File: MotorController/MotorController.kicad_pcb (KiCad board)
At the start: 2 copper layers, 55 x 45 mm, 35 parts, among them J1 4P4C, J2 AVR-ISP-10, J3 8P8C, J4 Screw_Terminal_01x02, Q1 Q_NMOS_GSD, SW1 SW_SPDT, SW2 SW_Push, U1 LD1117S50TR_SOT223, U2 MAX485E, U3 ATmega8A-AU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

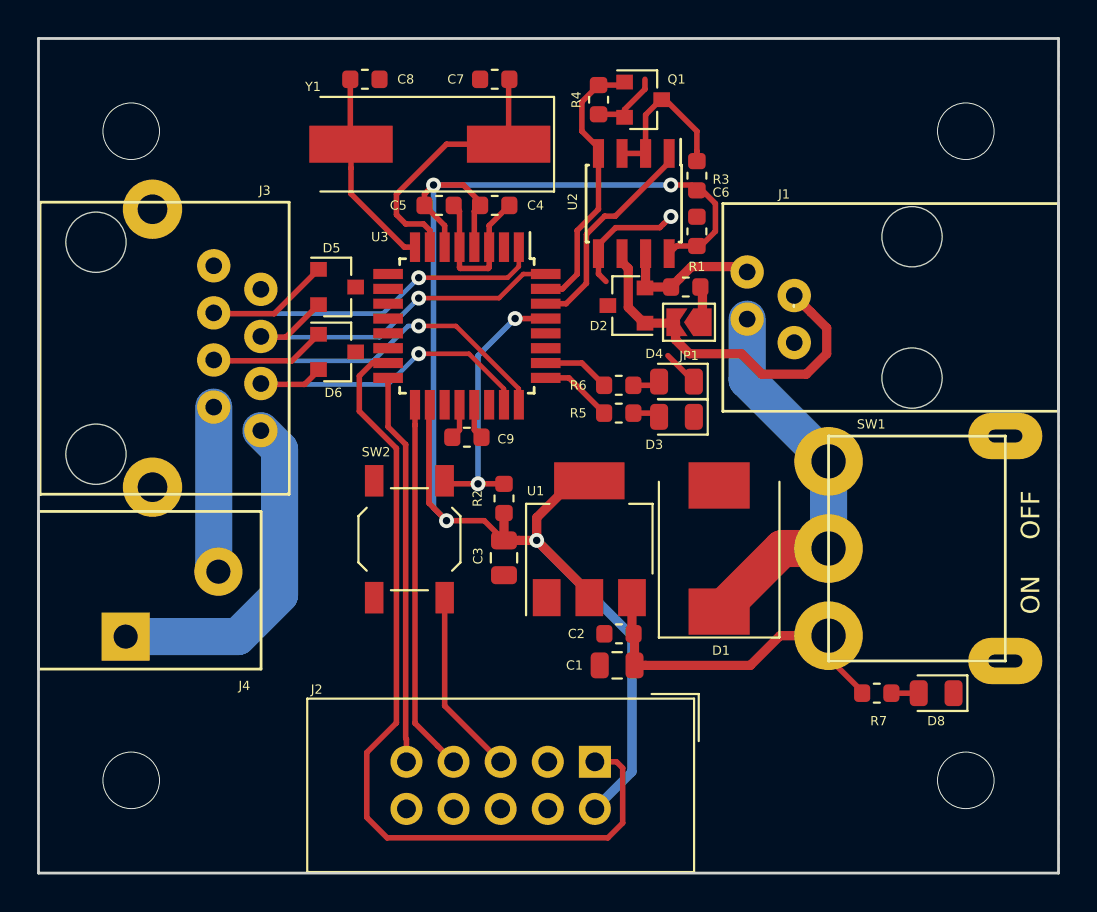
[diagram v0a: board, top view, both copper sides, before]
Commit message: First review. Fixed polygon pours, silkscreen and soldermask.
Squashed commit of the following:

commit 42a4a5d146683d2b2a8899b51cbc9eaef6797660
Author: Paweł <mackipawel@gmail.com>
Date:   Tue Apr 16 00:20:58 2019 +0200

    Changed solder mask design rules. Changed polygon pours clearence.

commit a27d25858da40b0edc55a62741cad58f571e73a1
Author: Paweł <mackipawel@gmail.com>
Date:   Sun Apr 14 15:00:25 2019 +0200

    Set via size to 0.3/0.6. Added silk screen descriptions in MotorDriver.

commit d55559f2128c74f860d75a89ad8b68139a6ba707
Author: Paweł <mackipawel@gmail.com>
Date:   Sun Apr 14 13:56:25 2019 +0200

    Added EcoTech logo in MotorController.
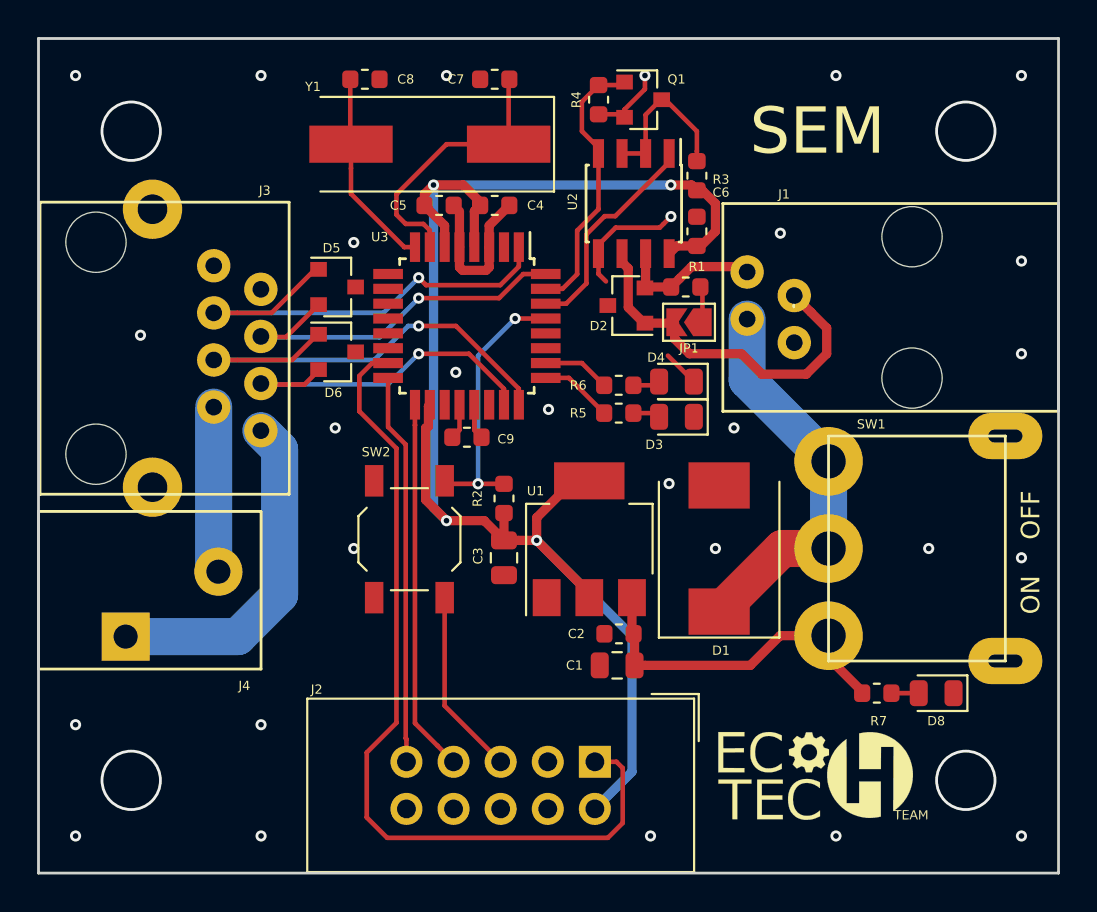
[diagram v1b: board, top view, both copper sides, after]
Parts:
- added G***: LOGO, Footprints:EcoTech, F.Cu at (117.0, 100.0)
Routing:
- net /A: track 20.1 -> 19.5 mm
- net GND: track 24.0 -> 24.1 mm, vias 1 -> 28
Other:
- net class Default: via_dia 0.8 -> 0.6; via_drill 0.4 -> 0.3
- net class Power added: clearance 0.2, trace_width 2, via_dia 0.6, via_drill 0.3
- net class Wide added: clearance 0.2, trace_width 0.5, via_dia 0.6, via_drill 0.3
- rule pad_to_mask_clearance: 0.051 -> 0.1
- rule solder_mask_min_width: 0.25 -> 0.2
- board text added: "SEM"

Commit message: Small changes in copper pours.
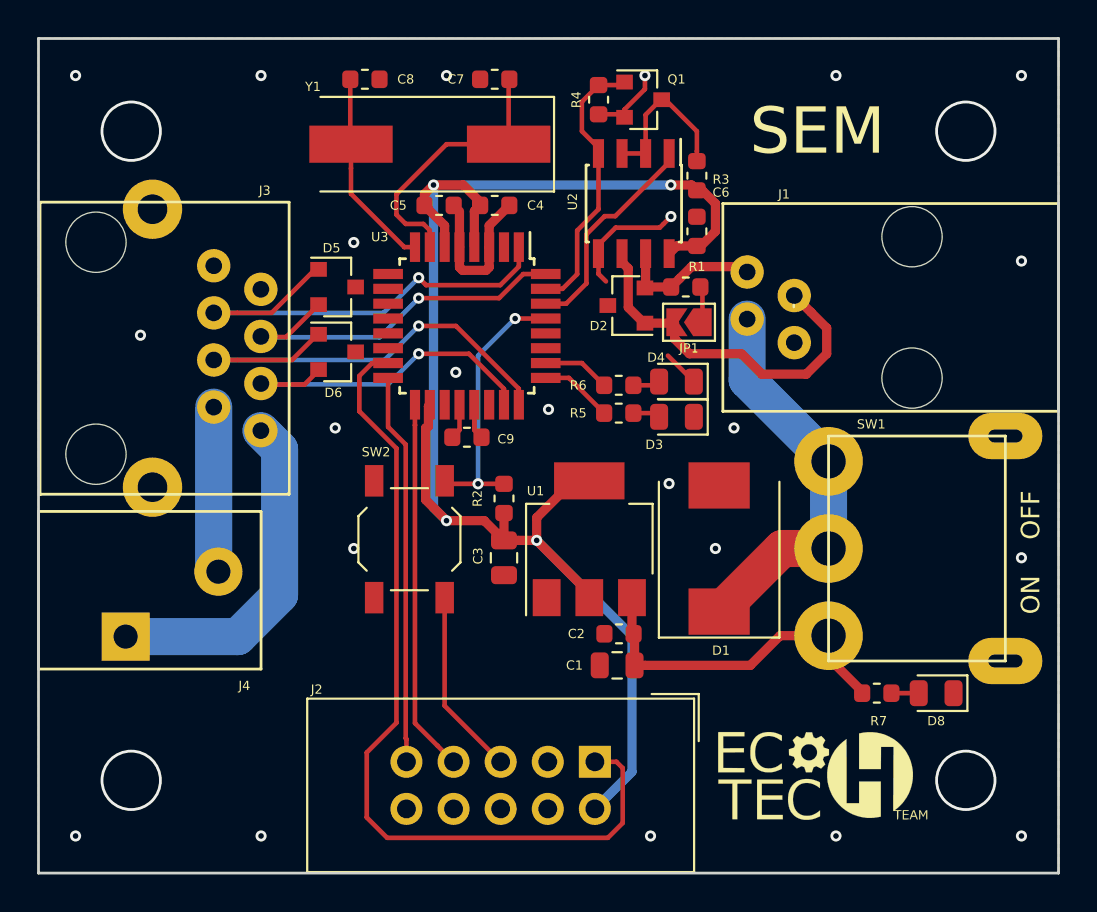
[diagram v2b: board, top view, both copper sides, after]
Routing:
- net GND: vias 28 -> 23
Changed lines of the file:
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@@
     (thickness 1.6)
     (drawings 7)
-    (tracks 284)
+    (tracks 278)
     (zones 0)
     (modules 36)
@@
   (via (at 128 88) (size 0.6) (drill 0.3) (layers F.Cu B.Cu) (net 10))
   (via (at 128 72) (size 0.6) (drill 0.3) (layers F.Cu B.Cu) (net 10))
-  (via (at 128 77) (size 0.6) (drill 0.3) (layers F.Cu B.Cu) (net 10))
   (via (at 109 84) (size 0.6) (drill 0.3) (layers F.Cu B.Cu) (net 10))
   (via (at 112.5 81) (size 0.6) (drill 0.3) (layers F.Cu B.Cu) (net 10))
   (via (at 111.5 87.5) (size 0.6) (drill 0.3) (layers F.Cu B.Cu) (net 10))
-  (via (at 123 87.5) (size 0.6) (drill 0.3) (layers F.Cu B.Cu) (net 10))
-  (via (at 115 70.5) (size 0.6) (drill 0.3) (layers F.Cu B.Cu) (net 10))
   (via (at 97.5 78) (size 0.6) (drill 0.3) (layers F.Cu B.Cu) (net 10))
   (via (at 102.5 80) (size 0.6) (drill 0.3) (layers F.Cu B.Cu) (net 10))
@@
   (via (at 80.5 76) (size 0.6) (drill 0.3) (layers F.Cu B.Cu) (net 10))
   (via (at 92 87.5) (size 0.6) (drill 0.3) (layers F.Cu B.Cu) (net 10))
-  (via (at 87 97) (size 0.6) (drill 0.3) (layers F.Cu B.Cu) (net 10))
-  (via (at 77 97) (size 0.6) (drill 0.3) (layers F.Cu B.Cu) (net 10))
   (segment (start 106.4375 62.5125) (end 106.6 62.35) (width 0.25) (layer F.Cu) (net 11))
   (segment (start 105.2 62.5125) (end 106.4375 62.5125) (width 0.25) (layer F.Cu) (net 11))
@@
   (segment (start 95.5 75.5) (end 95.5 75.5) (width 0.25) (layer F.Cu) (net 17))
   (via (at 95.5 75.5) (size 0.6) (drill 0.3) (layers F.Cu B.Cu) (net 17))
-  (segment (start 95.5 75.5) (end 94.934315 75.5) (width 0.25) (layer B.Cu) (net 17))
   (segment (start 85.722792 77.335) (end 84.45 77.335) (width 0.25) (layer F.Cu) (net 17))
   (segment (start 88.665 77.335) (end 85.722792 77.335) (width 0.25) (layer F.Cu) (net 17))
   (segment (start 90.1 75.95) (end 90.05 75.95) (width 0.25) (layer F.Cu) (net 17))
   (segment (start 90.05 75.95) (end 88.665 77.335) (width 0.25) (layer F.Cu) (net 17))
-  (segment (start 93.099315 77.335) (end 84.45 77.335) (width 0.25) (layer B.Cu) (net 17))
-  (segment (start 94.934315 75.5) (end 93.099315 77.335) (width 0.25) (layer B.Cu) (net 17))
+  (segment (start 93.665 77.335) (end 84.45 77.335) (width 0.25) (layer B.Cu) (net 17))
+  (segment (start 95.5 75.5) (end 93.665 77.335) (width 0.25) (layer B.Cu) (net 17))
   (segment (start 107.7 75.35) (end 109.3 75.35) (width 0.5) (layer F.Cu) (net 18))
   (segment (start 116.649999 74.759999) (end 115.75 73.86) (width 0.5) (layer F.Cu) (net 18))
@@
     (connect_pads (clearance 0.25))
     (min_thickness 0.25)
-    (fill yes (arc_segments 16) (thermal_gap 0.508) (thermal_bridge_width 0.508))
+    (fill yes (arc_segments 16) (thermal_gap 0.3) (thermal_bridge_width 0.4))
     (polygon
       (pts
@@
     (connect_pads (clearance 0.25))
     (min_thickness 0.25)
-    (fill yes (arc_segments 16) (thermal_gap 0.508) (thermal_bridge_width 0.508))
+    (fill yes (arc_segments 16) (thermal_gap 0.3) (thermal_bridge_width 0.4))
     (polygon
       (pts

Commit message: Removed Switches from bus devices and added mounting holes in schematics.
Squashed commit of the following:

commit 448b4f84a5f64686dc4334a0b6d81609891ca7cf
Author: Paweł <mackipawel@gmail.com>
Date:   Sun Apr 28 20:22:14 2019 +0200

    Added mouting holes to SystemSupply.

commit d45917b7024ecbe087cb8328a2c33d3ab10399ff
Author: Paweł <mackipawel@gmail.com>
Date:   Sun Apr 28 20:13:41 2019 +0200

    Added mouting holes to SafetySystem.

commit 6365380671305e2241dc821ec3b00ae08a997ac5
Author: Paweł <mackipawel@gmail.com>
Date:   Sun Apr 28 20:11:13 2019 +0200

    Added mouting holes to SafetySupply.

commit 00163d4bba61eb48f9ebb4c601b04017e78006be
Author: Paweł <mackipawel@gmail.com>
Date:   Sun Apr 28 20:06:38 2019 +0200

    Fixed MotorController.

commit ec0507ca51ef80aebbe2605505e7109beac59e98
Author: Paweł <mackipawel@gmail.com>
Date:   Sun Apr 28 19:54:40 2019 +0200

    Fixed MotorDriver.
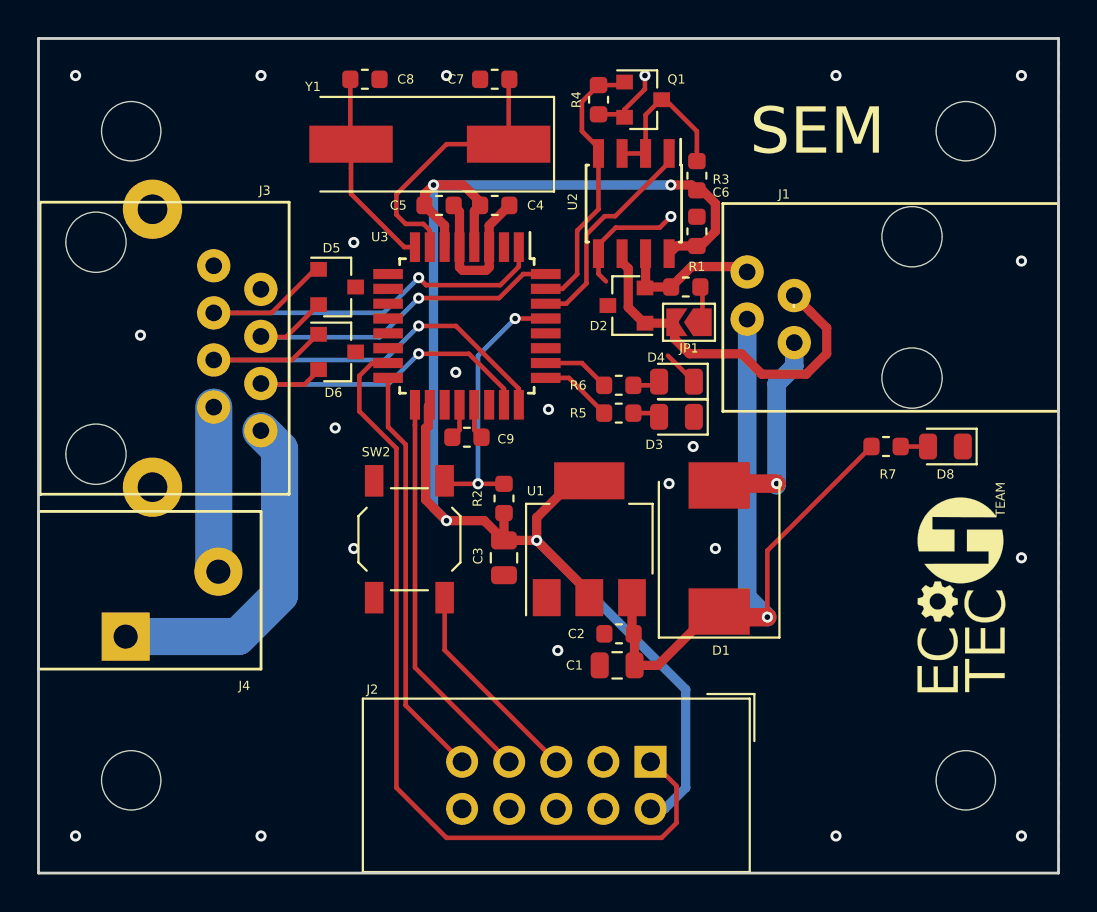
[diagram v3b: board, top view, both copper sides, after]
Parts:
- removed SW1: SW_SPDT, Footprints:5MS1S102AM6QE
- added H1: MountingHole, MountingHole:MountingHole_3.2mm_M3, F.Cu at (80.0, 65.0)
- added H2: MountingHole, MountingHole:MountingHole_3.2mm_M3, F.Cu at (80.0, 100.0)
- added H3: MountingHole, MountingHole:MountingHole_3.2mm_M3, F.Cu at (125.0, 65.0)
- added H4: MountingHole, MountingHole:MountingHole_3.2mm_M3, F.Cu at (125.0, 100.0)
- G1: renamed from G***; value LOGO -> EcoTechLogo
- moved D8 13.3 mm to (123.9, 82.0)
- moved R7 13.3 mm to (120.7, 82.0)
- moved G1 12.9 mm to (125.0, 89.9), turned to 90 degrees
- moved J2 3.00 mm to (108.0, 99.0)
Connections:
- D1 pad 1: Net-(D1-Pad1) -> +12V
- J1 pad 2: Net-(D1-Pad1) -> +12V
- J3 pad 0: GND -> (no net)
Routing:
- net +12V: track 18.7 -> 40.3 mm, vias 0 -> 1
- net Net-(D1-Pad1): track 21.5 -> 0.00 mm
- net GND: track 24.1 -> 35.3 mm, vias 23 -> 24
- net +5V: track 88.5 -> 90.1 mm
- net /SCK: track 20.1 -> 21.4 mm
- net /RST: track 24.8 -> 26.0 mm
- net /MISO: track 21.1 -> 22.4 mm
- net Net-(J2-Pad3): track 0.00 -> 1.16 mm
- net /MOSI: track 46.3 -> 45.4 mm
- net (no net): vias 4 -> 0
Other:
- board text removed: "OFF"
- board text removed: "ON"

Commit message: Added testpoints.
Squashed commit of the following:

commit b78741095f1293168643ce5f943c13a7eb09b318
Author: Paweł <mackipawel@gmail.com>
Date:   Thu May 2 10:22:35 2019 +0200

    Added testpoints to remaining projects.

commit d708f3fd02ddff10684a41533d76b9b66ea6c8f4
Author: Paweł <mackipawel@gmail.com>
Date:   Sun Apr 28 23:49:47 2019 +0200

    Added testpoints in MotorController and MotorDriver.
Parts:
- added TP1: TestPoint, TestPoint:TestPoint_Loop_D1.80mm_Drill1.0mm_Beaded, F.Cu at (118.0, 98.0)
- added TP2: TestPoint, TestPoint:TestPoint_Loop_D1.80mm_Drill1.0mm_Beaded, F.Cu at (100.8, 93.5)
- added TP3: TestPoint, TestPoint:TestPoint_Loop_D1.80mm_Drill1.0mm_Beaded, F.Cu at (118.0, 91.0)
- added TP4: TestPoint, TestPoint:TestPoint_Loop_D1.80mm_Drill1.0mm_Beaded, F.Cu at (114.0, 65.0)
- added TP5: TestPoint, TestPoint:TestPoint_Loop_D1.80mm_Drill1.0mm_Beaded, F.Cu at (118.0, 65.0)
- moved G1 0.90 mm to (124.1, 89.9)
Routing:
- net /A: track 19.5 -> 29.3 mm
- net /B: track 7.97 -> 15.9 mm
- net +5V: track 90.1 -> 95.6 mm
- net +12V: track 40.3 -> 44.1 mm

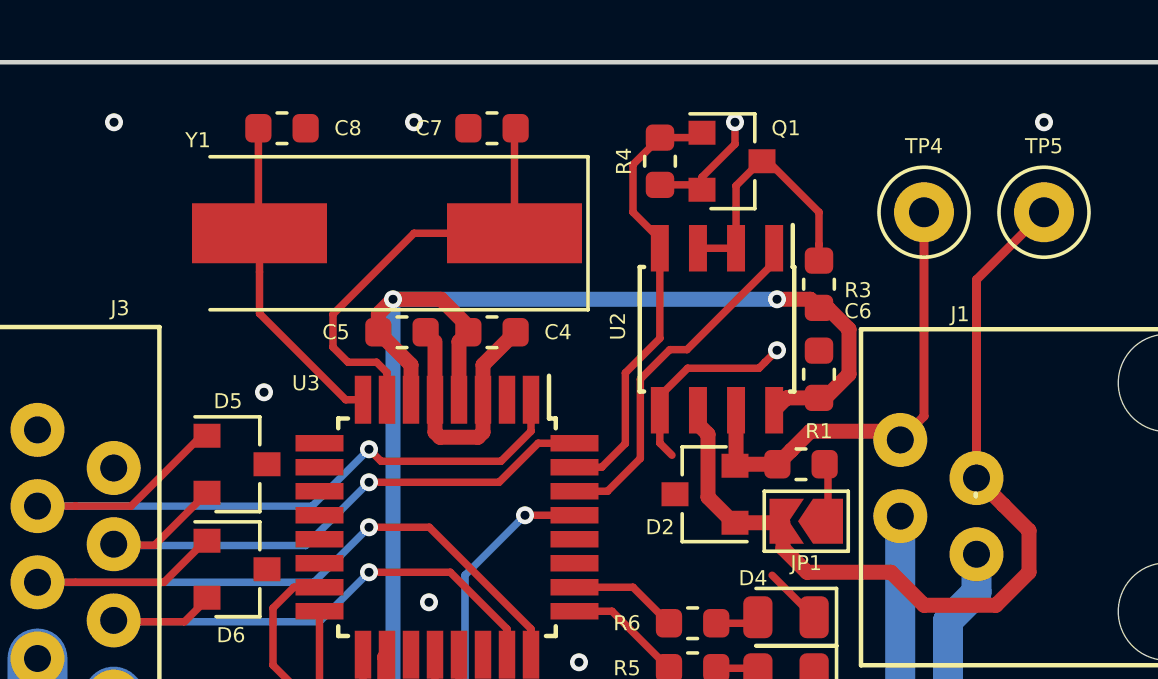
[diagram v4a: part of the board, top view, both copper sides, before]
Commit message: Added 3D models to the library
Squashed commit of the following:

commit 8070c09fc3d8f70a7cb84d0f12b6782c2c87c14c
Author: Paweł <mackipawel@gmail.com>
Date:   Mon May 6 20:26:56 2019 +0200

    Added SystemSupply 3d models.

commit 94ef8708632c7bc91211bc6ded4e0c8fb9ccef4a
Author: Paweł <mackipawel@gmail.com>
Date:   Mon May 6 01:08:52 2019 +0200

    Added 3D models to SystemSupply.

commit eb394d70be979be958e4acab21accb1817e8e0e5
Author: Paweł <mackipawel@gmail.com>
Date:   Mon May 6 00:55:39 2019 +0200

    Added 3D model to MotorController.

commit fd89e01e0ef36f85afad3e8686d3deffdf36454d
Author: Paweł <mackipawel@gmail.com>
Date:   Mon May 6 00:40:56 2019 +0200

    Added 3D models in MotorDriver.

commit 899d106fa8d45578189a4955328047d8f9558beb
Author: Paweł <mackipawel@gmail.com>
Date:   Mon May 6 00:09:40 2019 +0200

    Added 3D models to SafetySupply.

commit 06c807994bb47431d2802a96796741a0e8fb9ae5
Author: Paweł <mackipawel@gmail.com>
Date:   Sun May 5 23:17:48 2019 +0200

    Added 3D models to SafetySystem.
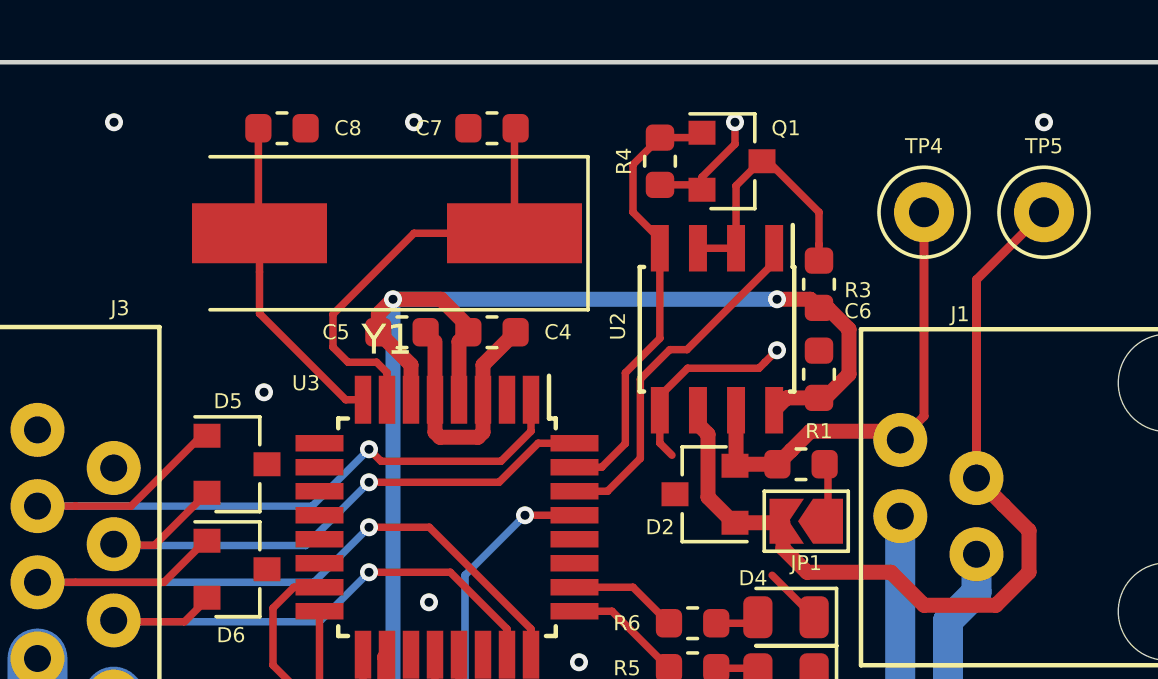
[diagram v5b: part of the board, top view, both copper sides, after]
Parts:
- Y1: footprint Crystal:Crystal_SMD_HC49-SD -> Footprints:Crystal_SMD_HC49-SD
